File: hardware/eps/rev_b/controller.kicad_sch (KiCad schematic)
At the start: 15 parts, among them U100 STM32G0B1KET6N, Y100 ECS-3225MV-160-BN-TR

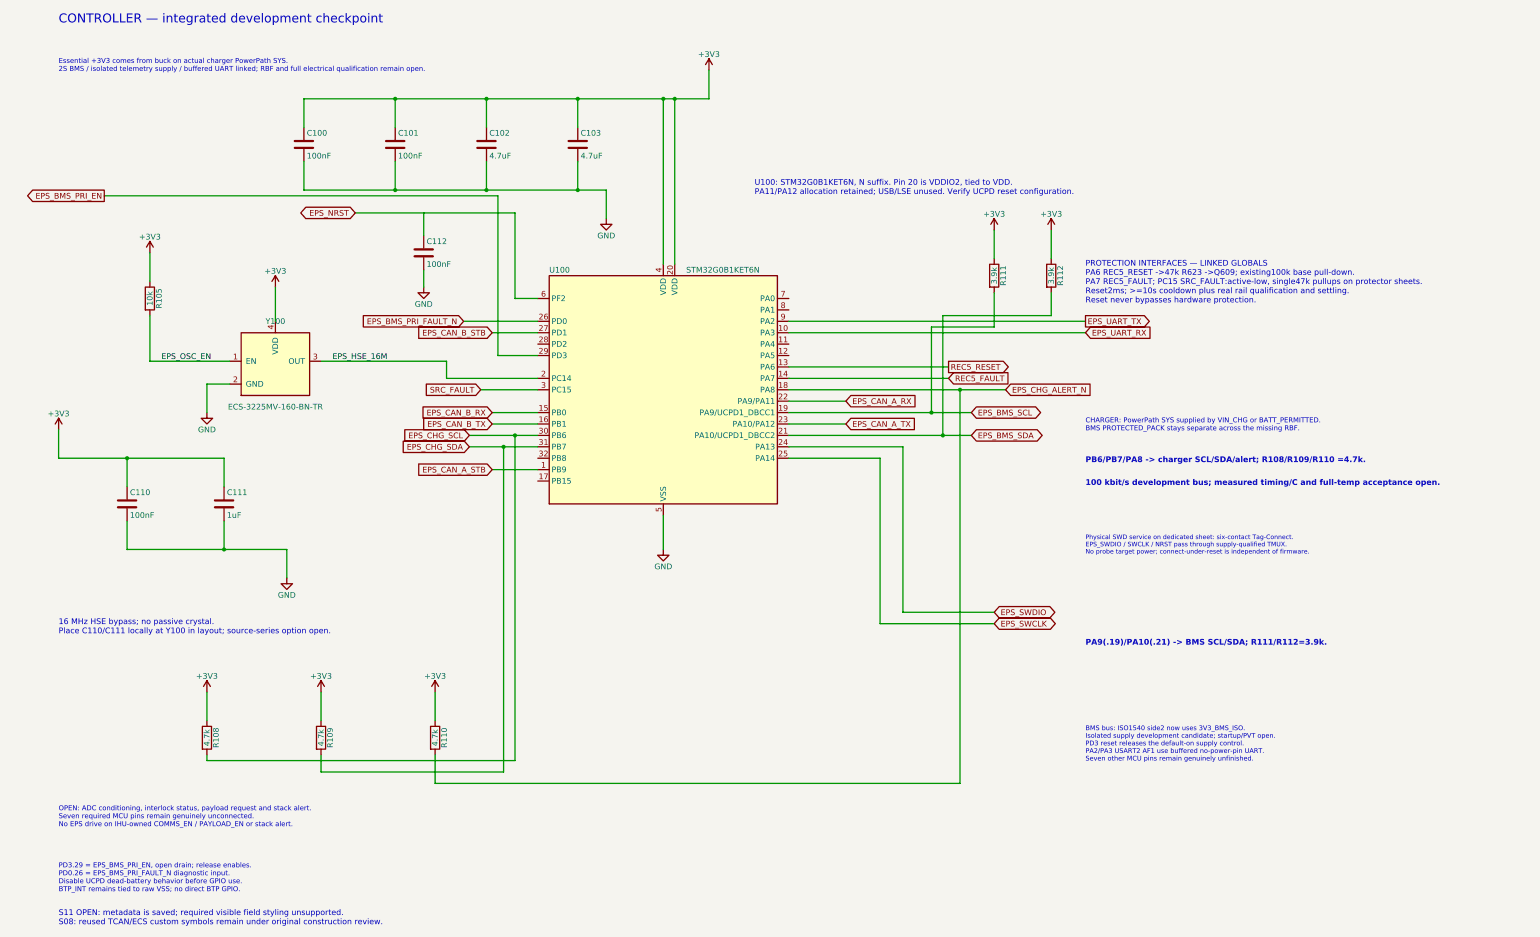
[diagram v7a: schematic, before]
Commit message: Integrate EPS rail telemetry and record source-guard limits
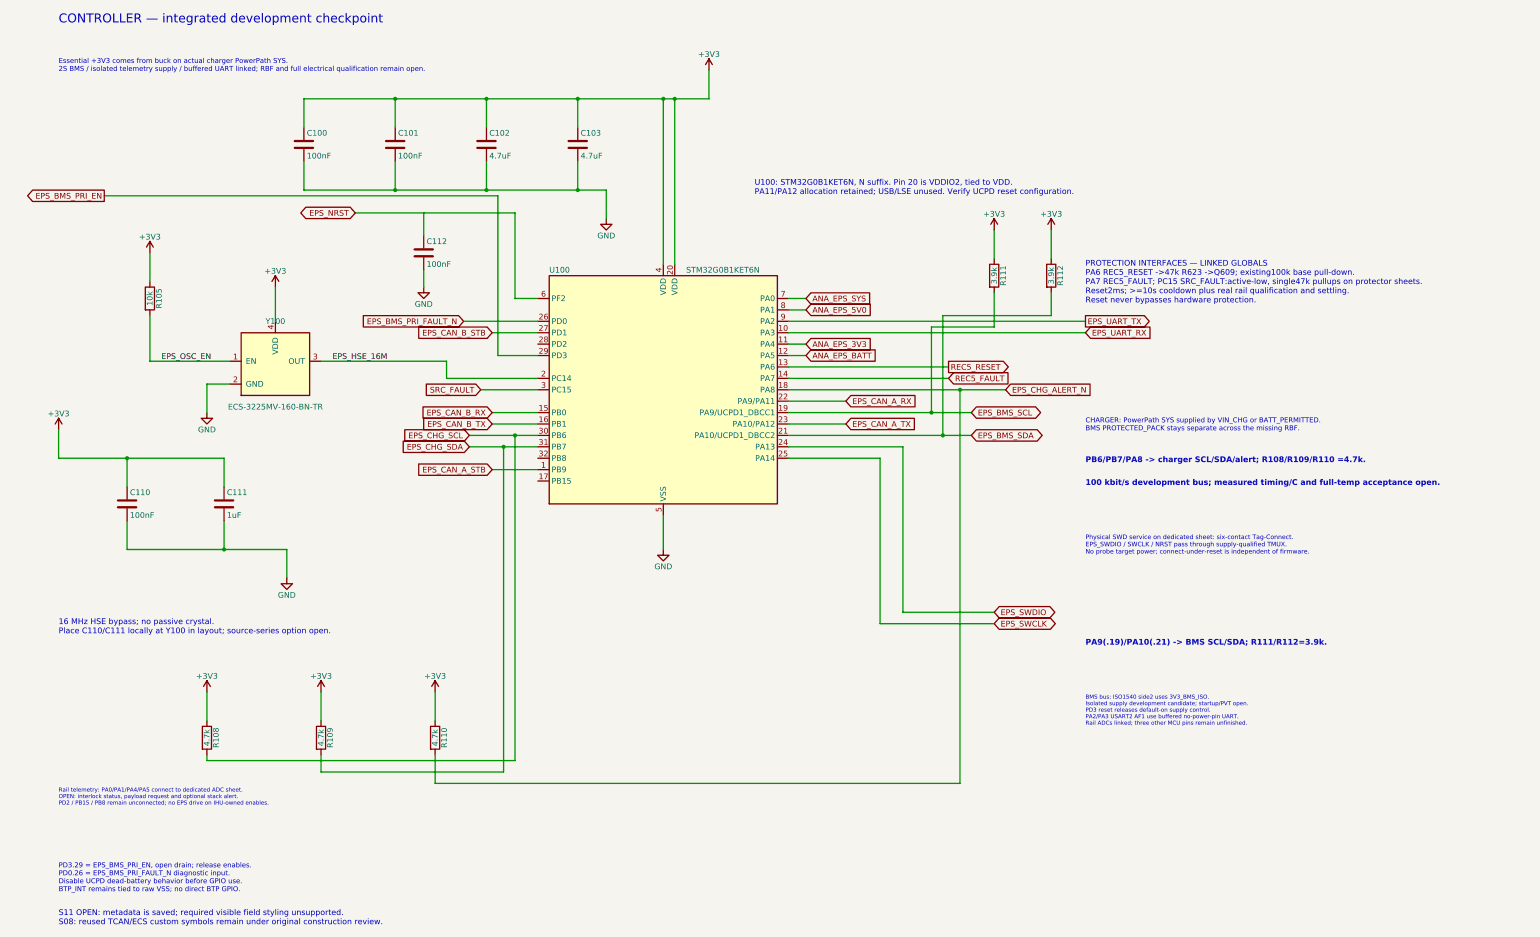
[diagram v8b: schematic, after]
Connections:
- net ANA_EPS_3V3: now reaches U100.11 (PA4)
- net ANA_EPS_BATT: now reaches U100.12 (PA5)
- net ANA_EPS_SYS: now reaches U100.7 (PA0)
- net ANA_EPS_5V0: now reaches U100.8 (PA1)
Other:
- note added: "BMS bus: ISO1540 side2 uses 3V3_BMS_ISO. Isolated supply development candidate; startup/PVT open. PD3 reset releases default-on supply control. PA2/PA3 USART2 AF1 use buffered no-power-pin UART. Rail ADCs linked; three other MCU pins remain unfinished."
- note added: "Rail telemetry: PA0/PA1/PA4/PA5 connect to dedicated ADC sheet. OPEN: interlock status, payload request and optional stack alert. PD2 / PB15 / PB8 remain unconnected; no EPS drive on IHU-owned enables."
- note removed: "BMS bus: ISO1540 side2 now uses 3V3_BMS_ISO. Isolated supply development candidate; startup/PVT open. PD3 reset releases the default-on supply control. PA2/PA3 USART2 AF1 use buffered no-power-pin UART. Seven other MCU pins remain genuinely unfinished."
- note removed: "OPEN: ADC conditioning, interlock status, payload request and stack alert. Seven required MCU pins remain genuinely unconnected. No EPS drive on IHU-owned COMMS_EN / PAYLOAD_EN or stack alert."
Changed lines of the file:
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@@
+		)
+	)
+	(wire
+		(pts
+			(xy 187.96 85.09)
+			(xy 191.77 85.09)
+		)
+	)
+	(wire
+		(pts
+			(xy 187.96 87.63)
+			(xy 191.77 87.63)
+		)
+	)
+	(wire
+		(pts
+			(xy 187.96 95.25)
+			(xy 191.77 95.25)
+		)
+	)
+	(wire
+		(pts
+			(xy 187.96 97.79)
+			(xy 191.77 97.79)
 		)
 	)
@@
 		)
 	)
-	(text "BMS bus: ISO1540 side2 now uses 3V3_BMS_ISO.\nIsolated supply development candidate; startup/PVT open.\nPD3 reset releases the default-on supply control.\nPA2/PA3 USART2 AF1 use buffered no-power-pin UART.\nSeven other MCU pins remain genuinely unfinished."
-		(at 254 180.34 0)
-		(effects
-			(font
-				(size 1.05 1.05)
-			)
-			(justify left top)
-		)
-	)
 	(text "Essential +3V3 comes from buck on actual charger PowerPath SYS.\n2S BMS / isolated telemetry supply / buffered UART linked; RBF and full electrical qualification remain open."
 		(at 25.4 31.75 0)
@@
 		)
 	)
-	(text "OPEN: ADC conditioning, interlock status, payload request and stack alert.\nSeven required MCU pins remain genuinely unconnected.\nNo EPS drive on IHU-owned COMMS_EN / PAYLOAD_EN or stack alert."
-		(at 25.4 198.12 0)
-		(effects
-			(font
-				(size 1.1 1.1)
-			)
-			(justify left top)
+	(text "Physical SWD service on dedicated sheet: six-contact Tag-Connect.\nEPS_SWDIO / SWCLK / NRST pass through supply-qualified TMUX.\nNo probe target power; connect-under-reset is independent of firmware."
+		(at 254 142.24 0)
+		(effects
+			(font
+				(size 1 1)
+			)
+			(justify left bottom)
 		)
 	)
@@
 		)
 	)
-  (text "Physical SWD service on dedicated sheet: six-contact Tag-Connect.\nEPS_SWDIO / SWCLK / NRST pass through supply-qualified TMUX.\nNo probe target power; connect-under-reset is independent of firmware."
-    (at 254 142.24 0)
-    (effects (font (size 1 1)) (justify left bottom))
+	(global_label "ANA_EPS_SYS"
+		(shape input)
+		(at 191.77 85.09 0)
+		(effects
+			(font
+				(size 1.27 1.27)
+			)
+			(justify left)
+		)
+	)
+	(global_label "ANA_EPS_5V0"
+		(shape input)
+		(at 191.77 87.63 0)
+		(effects
+			(font
+				(size 1.27 1.27)
+			)
+			(justify left)
+		)
+	)
+	(global_label "ANA_EPS_3V3"
+		(shape input)
+		(at 191.77 95.25 0)
+		(effects
+			(font
+				(size 1.27 1.27)
+			)
+			(justify left)
+		)
+	)
+	(global_label "ANA_EPS_BATT"
+		(shape input)
+		(at 191.77 97.79 0)
+		(effects
+			(font
+				(size 1.27 1.27)
+			)
+			(justify left)
+		)
+	)
+  (text "BMS bus: ISO1540 side2 uses 3V3_BMS_ISO.\nIsolated supply development candidate; startup/PVT open.\nPD3 reset releases default-on supply control.\nPA2/PA3 USART2 AF1 use buffered no-power-pin UART.\nRail ADCs linked; three other MCU pins remain unfinished."
+    (at 254 180.34 0)
+    (effects (font (size 0.9 0.9)) (justify left bottom))
+  )
+  (text "Rail telemetry: PA0/PA1/PA4/PA5 connect to dedicated ADC sheet.\nOPEN: interlock status, payload request and optional stack alert.\nPD2 / PB15 / PB8 remain unconnected; no EPS drive on IHU-owned enables."
+    (at 25.4 198.12 0)
+    (effects (font (size 0.9 0.9)) (justify left bottom))
   )
 	(symbol
